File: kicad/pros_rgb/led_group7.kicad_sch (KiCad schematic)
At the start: 8 parts

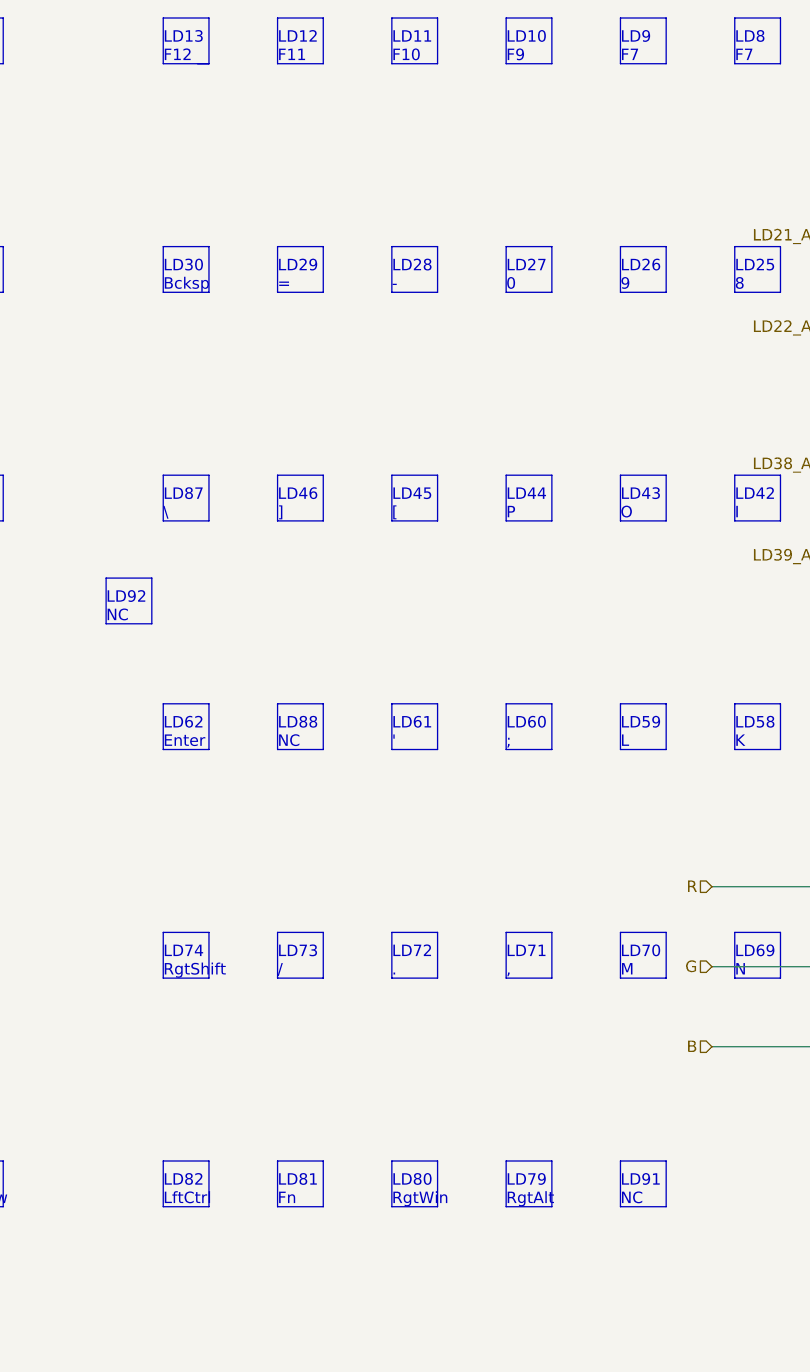
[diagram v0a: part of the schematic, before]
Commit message: kicad/pros_rgb: fix typos
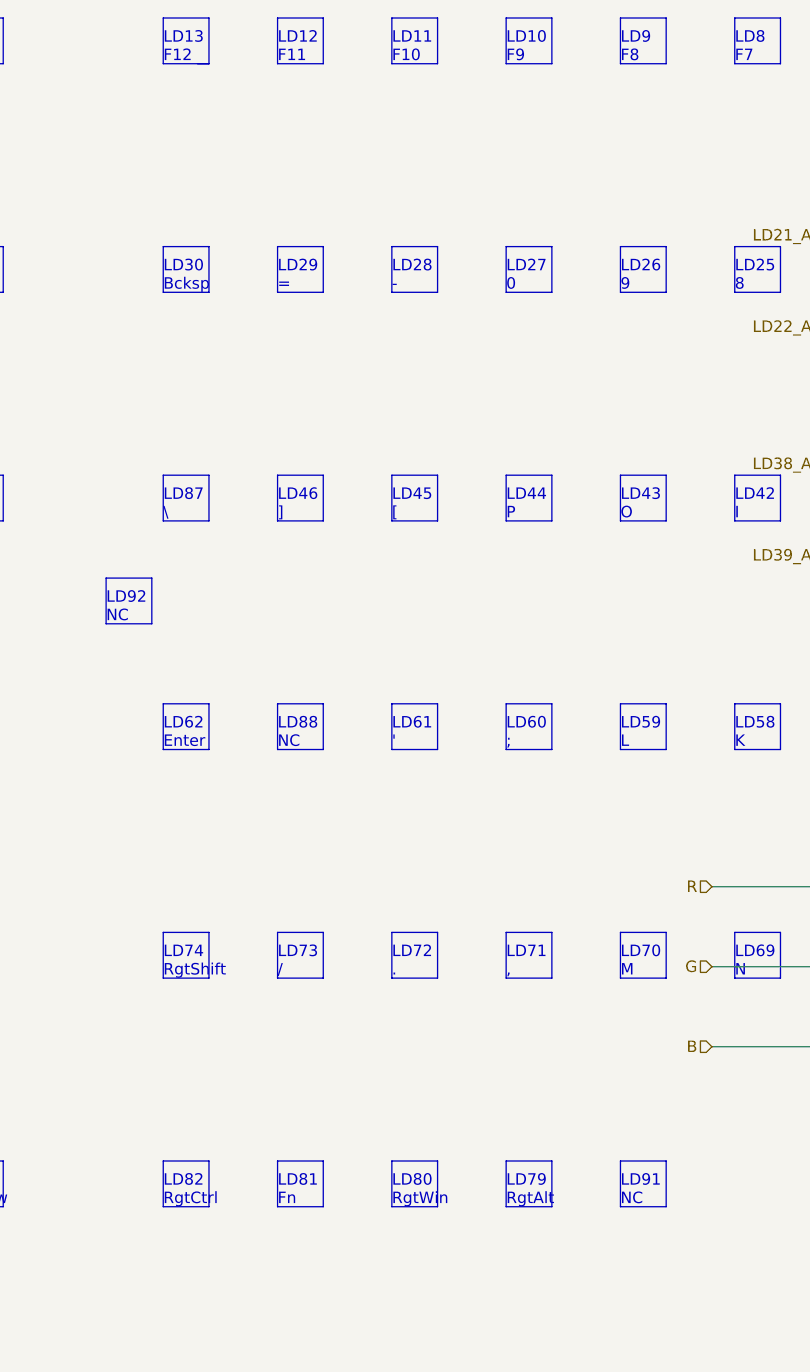
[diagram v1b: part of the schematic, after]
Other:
- note added: "LD82 RgtCtrl"
- note added: "LD9 F8"
- note removed: "LD82 LftCtrl"
- note removed: "LD9 F7"
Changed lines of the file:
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@@
     (effects (font (size 1.27 1.27)) (justify left bottom))
   )
-  (text "LD82\nLftCtrl" (at 106.68 156.21 0)
+  (text "LD82\nRgtCtrl" (at 106.68 156.21 0)
     (effects (font (size 1.27 1.27)) (justify left bottom))
   )
@@
     (effects (font (size 1.27 1.27)) (justify left bottom))
   )
-  (text "LD9\nF7" (at 157.48 29.21 0)
+  (text "LD9\nF8" (at 157.48 29.21 0)
     (effects (font (size 1.27 1.27)) (justify left bottom))
   )

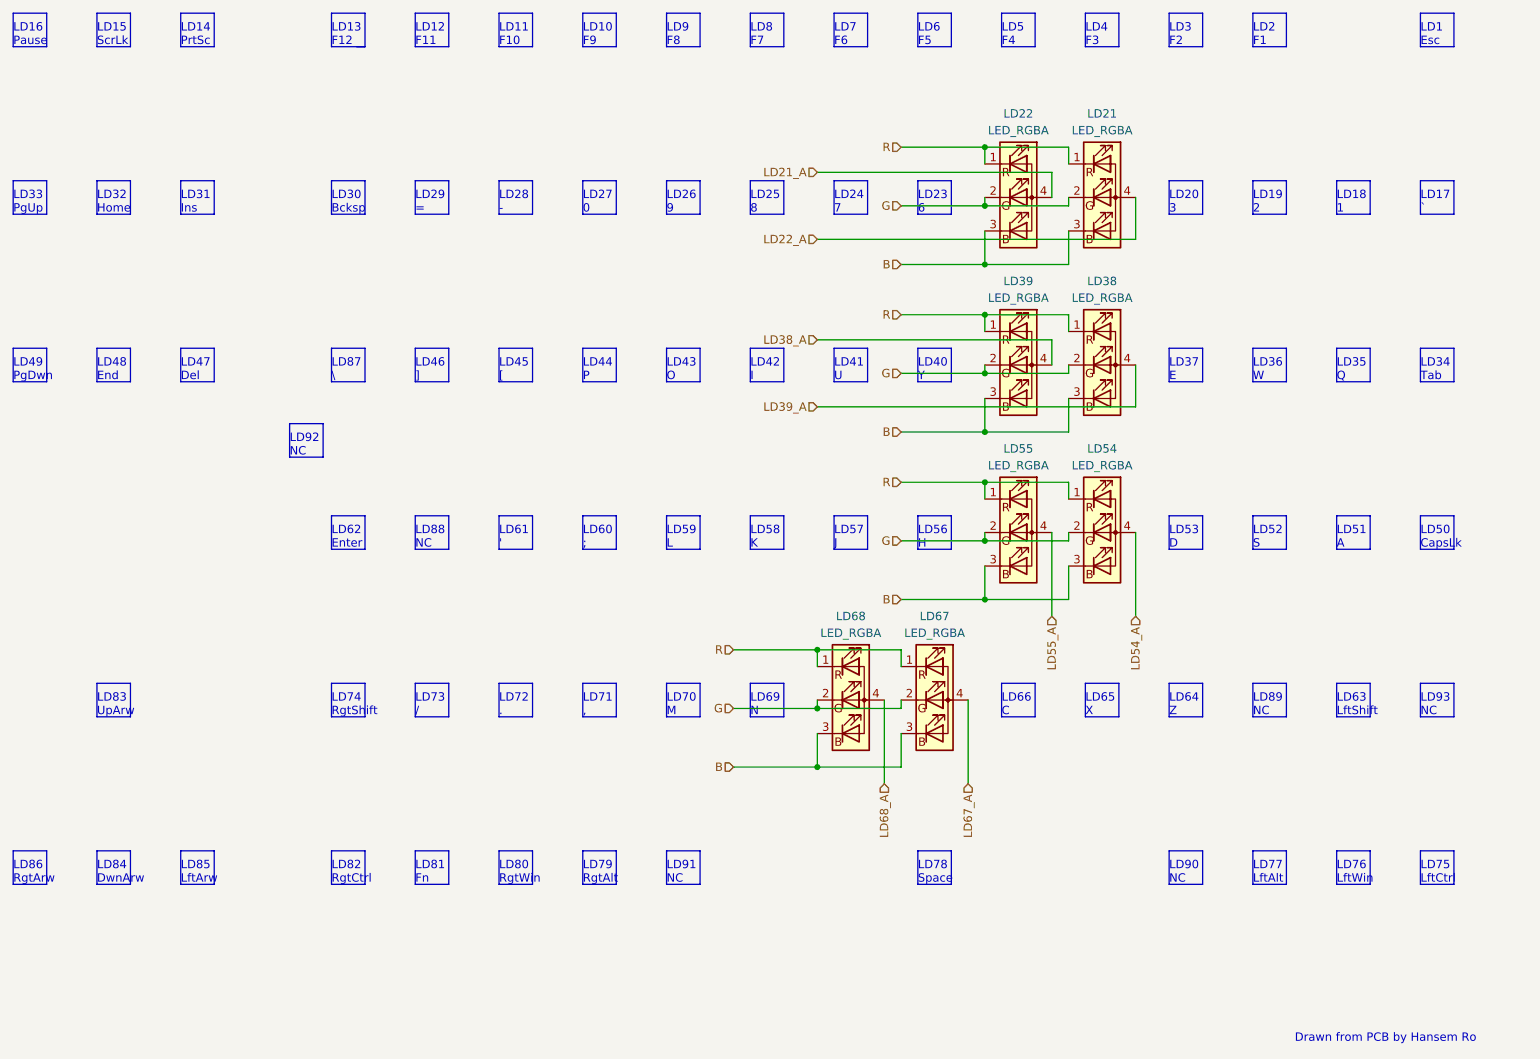
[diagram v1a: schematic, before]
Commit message: kicad/pros_rgb: order led groups by channel number
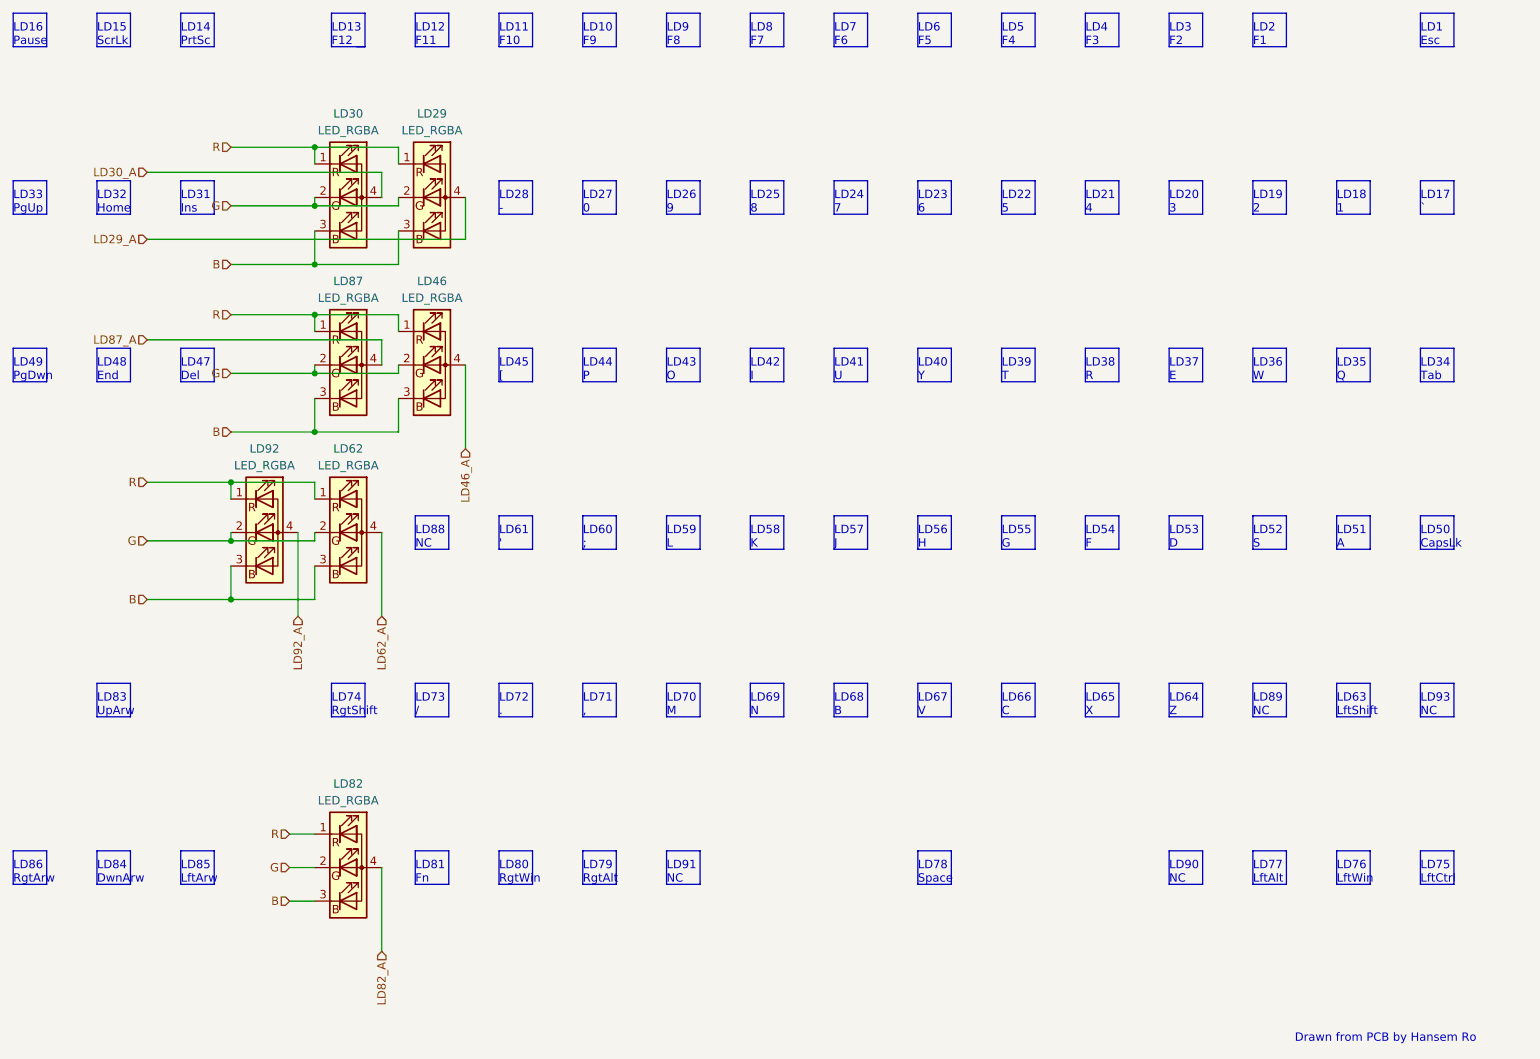
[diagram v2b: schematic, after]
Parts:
- removed LD21, LD22, LD38, LD39, LD54, LD55, LD67, LD68: LED_RGBA, symbol Device:LED_RGBA
- added LD29, LD30, LD46, LD62, LD82, LD87, LD92: LED_RGBA, symbol Device:LED_RGBA
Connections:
- net B: now also LD29.3 (BK), LD30.3 (BK), LD46.3 (BK), LD62.3 (BK), LD82.3 (BK), LD87.3 (BK), LD92.3 (BK)
- net G: now also LD29.2 (GK), LD30.2 (GK), LD46.2 (GK), LD62.2 (GK), LD82.2 (GK), LD87.2 (GK), LD92.2 (GK)
- net R: now also LD29.1 (RK), LD30.1 (RK), LD46.1 (RK), LD62.1 (RK), LD82.1 (RK), LD87.1 (RK), LD92.1 (RK)
- new net LD29_A: LD29.4 (A)
- new net LD30_A: LD30.4 (A)
- new net LD46_A: LD46.4 (A)
- new net LD62_A: LD62.4 (A)
- new net LD82_A: LD82.4 (A)
- new net LD87_A: LD87.4 (A)
- new net LD92_A: LD92.4 (A)
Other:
- note added: "LD21 4"
- note added: "LD22 5"
- note added: "LD38 R"
- note added: "LD39 T"
- note added: "LD54 F"
- note added: "LD55 G"
- note added: "LD67 V"
- note added: "LD68 B"
- note removed: "LD29 ="
- note removed: "LD30 Bcksp"
- note removed: "LD46 ]"
- note removed: "LD62 Enter"
- note removed: "LD82 RgtCtrl"
- note removed: "LD87 \"
- note removed: "LD92 NC"
